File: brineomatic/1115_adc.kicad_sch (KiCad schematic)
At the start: 5 parts, among them U3 ADS1115IDGSR

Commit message: tmc2209 driver schematic checked and laid out nicely.
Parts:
- renumbered C7 to C4, C8 to C5, U3 to U1
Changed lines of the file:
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@@
 		(on_board yes)
 		(dnp no)
-		(property "Reference" "C7"
+		(property "Reference" "C4"
 			(at 184.15 80.0163 0)
 			(effects
@@
 			(project "brineomatic"
 				(path "/96477ae2-ef08-48f3-8dd4-fe4478541f68/64f85b9c-b5dc-4ec9-9075-ce977ed1cba6"
-					(reference "C7")
+					(reference "C4")
 					(unit 1)
 				)
@@
 		(on_board yes)
 		(dnp no)
-		(property "Reference" "C8"
+		(property "Reference" "C5"
 			(at 195.58 80.0163 0)
 			(effects
@@
 			(project "brineomatic"
 				(path "/96477ae2-ef08-48f3-8dd4-fe4478541f68/64f85b9c-b5dc-4ec9-9075-ce977ed1cba6"
-					(reference "C8")
+					(reference "C5")
 					(unit 1)
 				)
@@
 		(dnp no)
 		(fields_autoplaced yes)
-		(property "Reference" "#PWR020"
+		(property "Reference" "#PWR021"
 			(at 127 69.85 0)
 			(effects
@@
 			(project "brineomatic"
 				(path "/96477ae2-ef08-48f3-8dd4-fe4478541f68/64f85b9c-b5dc-4ec9-9075-ce977ed1cba6"
-					(reference "#PWR020")
+					(reference "#PWR021")
 					(unit 1)
 				)
@@
 		(dnp no)
 		(fields_autoplaced yes)
-		(property "Reference" "U3"
+		(property "Reference" "U1"
 			(at 129.1941 71.12 0)
 			(effects
@@
 			(project ""
 				(path "/96477ae2-ef08-48f3-8dd4-fe4478541f68/64f85b9c-b5dc-4ec9-9075-ce977ed1cba6"
-					(reference "U3")
+					(reference "U1")
 					(unit 1)
 				)
@@
 		(dnp no)
 		(fields_autoplaced yes)
-		(property "Reference" "#PWR021"
+		(property "Reference" "#PWR022"
 			(at 127 105.41 0)
 			(effects
@@
 			(project ""
 				(path "/96477ae2-ef08-48f3-8dd4-fe4478541f68/64f85b9c-b5dc-4ec9-9075-ce977ed1cba6"
-					(reference "#PWR021")
-					(unit 1)
-				)
+					(reference "#PWR022")
+					(unit 1)
+				)

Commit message: worked on bom for rev b prototype run
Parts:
- C4: LCSC C49678 -> (none)
- C5: LCSC C1952580 -> (none)
- R15, R16: LCSC C114561 -> (none)
- U1: LCSC (none) -> C37593
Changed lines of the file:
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@@
 			)
 		)
-		(property "LCSC" "C49678"
+		(property "LCSC" ""
 			(at 181.61 81.28 0)
 			(effects
@@
 			)
 		)
-		(property "LCSC" "C1952580"
+		(property "LCSC" ""
 			(at 193.04 81.28 0)
 			(effects
@@
 			)
 		)
-		(property "LCSC" "C114561"
+		(property "LCSC" ""
 			(at 154.94 81.28 0)
 			(effects
@@
 			)
 		)
-		(property "LCSC" ""
+		(property "LCSC" "C37593"
 			(at 127 86.36 0)
 			(effects
@@
 			)
 		)
-		(property "LCSC" "C114561"
+		(property "LCSC" ""
 			(at 165.1 81.28 0)
 			(effects

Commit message: added qwiic i2c connector
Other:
- note added: "ADC"
- title: (none) -> https://github.com/hoeken/brineomatic
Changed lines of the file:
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@@
 	(generator_version "9.0")
 	(paper "A4")
+	(title_block
+		(title "https://github.com/hoeken/brineomatic")
+		(date "2025-08-28")
+		(rev "B")
+	)
+	(rectangle
+		(start 96.52 51.435)
+		(end 207.645 109.855)
+		(stroke
+			(width 0)
+			(type default)
+		)
+		(fill
+			(type none)
+		)
+	)
+	(text "ADC"
+		(exclude_from_sim no)
+		(at 99.314 55.118 0)
+		(effects
+			(font
+				(size 2 2)
+				(thickness 0.4)
+				(bold yes)
+			)
+			(justify left)
+		)
+	)
 	(junction
 		(at 165.1 67.31)

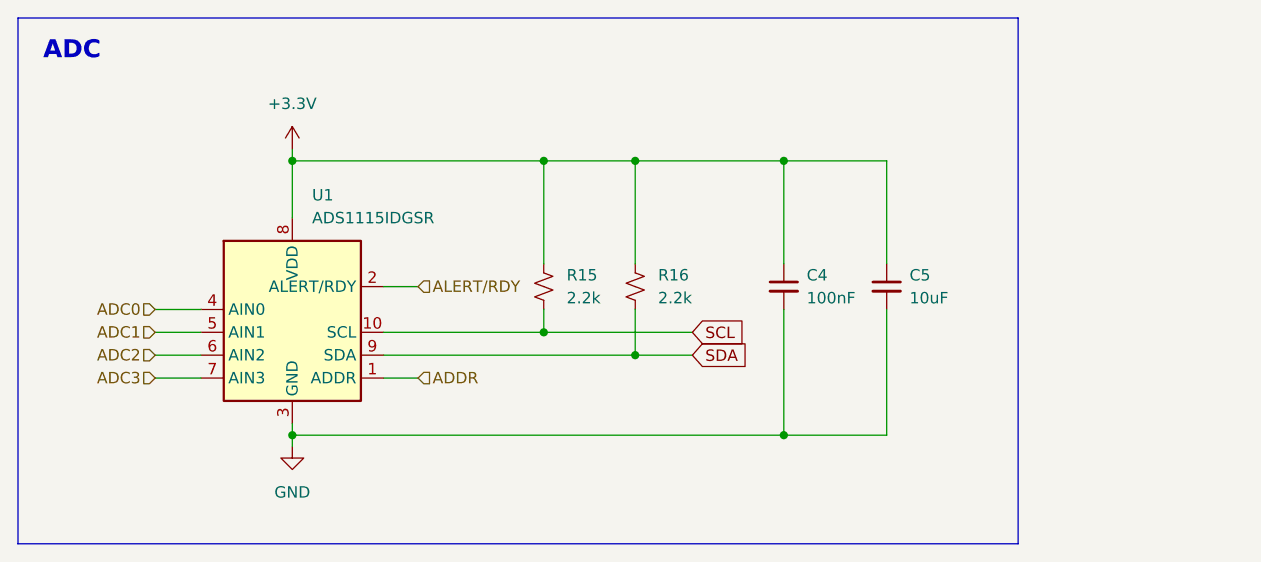
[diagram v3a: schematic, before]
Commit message: added pullup resistor to adc alert
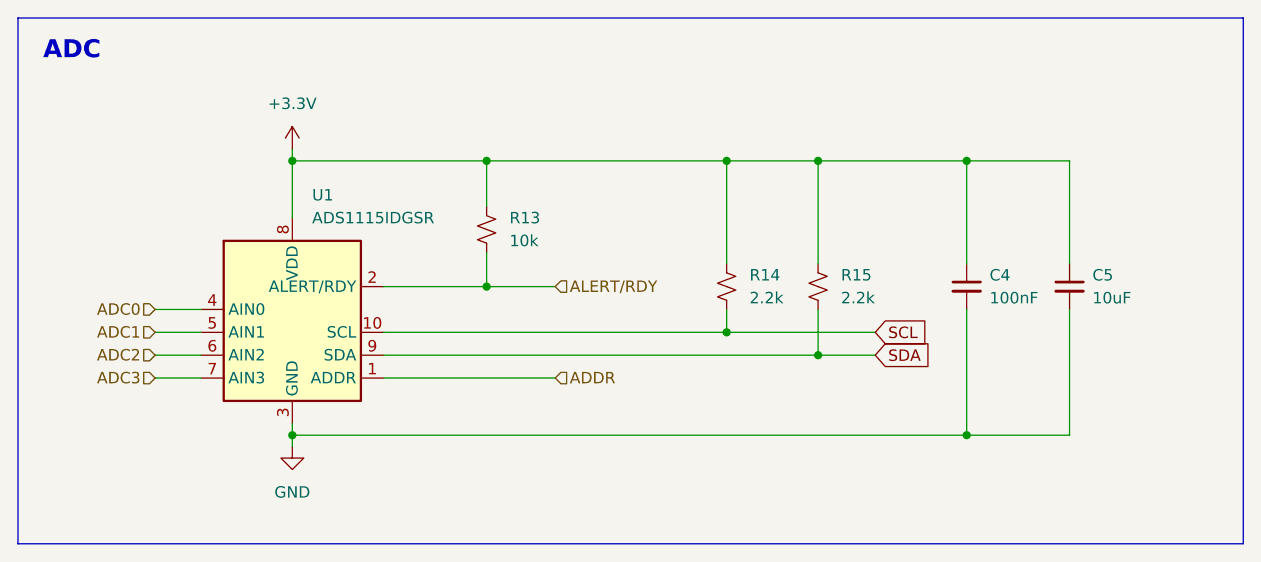
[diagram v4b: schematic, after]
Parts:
- added R13: 10k, Resistor_SMD:R_0603_1608Metric, symbol Device:R_Small_US
- renumbered R15 to R14, R16 to R15
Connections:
- net +3.3V: now also R13.2
- net ALERT/RDY: now also R13.1
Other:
- moved on the sheet: C4, C5, R14, R15

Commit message: board fully routed first pass.
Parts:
- added TP1, TP2: ~, TestPoint:TestPoint_THTPad_D1.5mm_Drill0.7mm, symbol Connector:TestPoint
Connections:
- net SCL: now also TP1.1
- net SDA: now also TP2.1

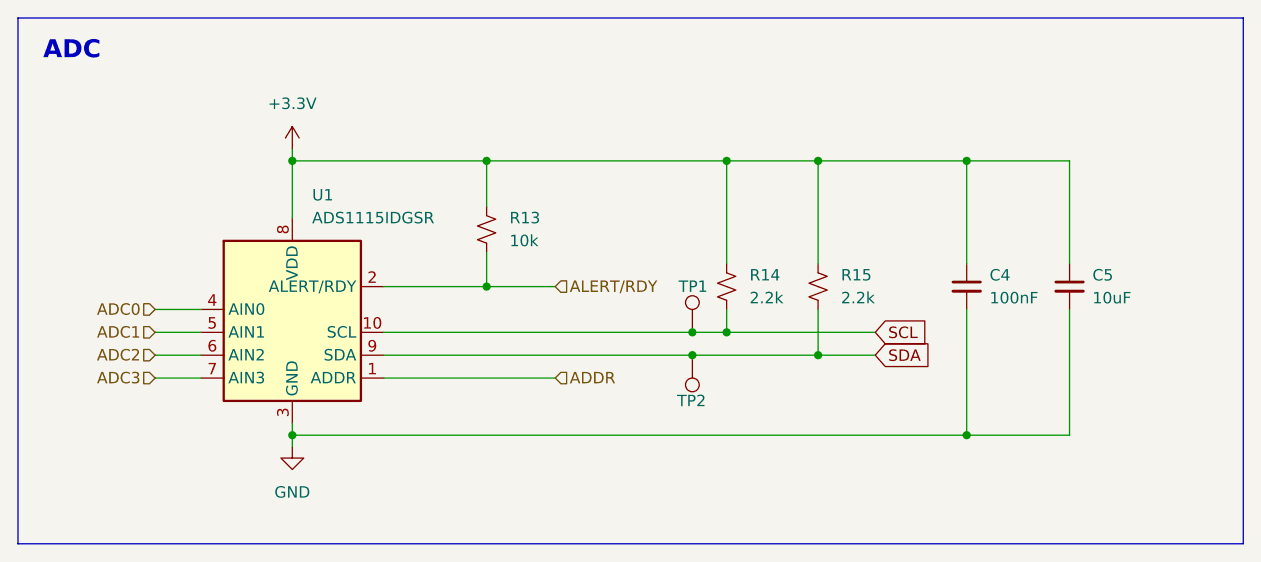
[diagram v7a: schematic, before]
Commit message: more esd protection, drc passing, silkscreen fixed
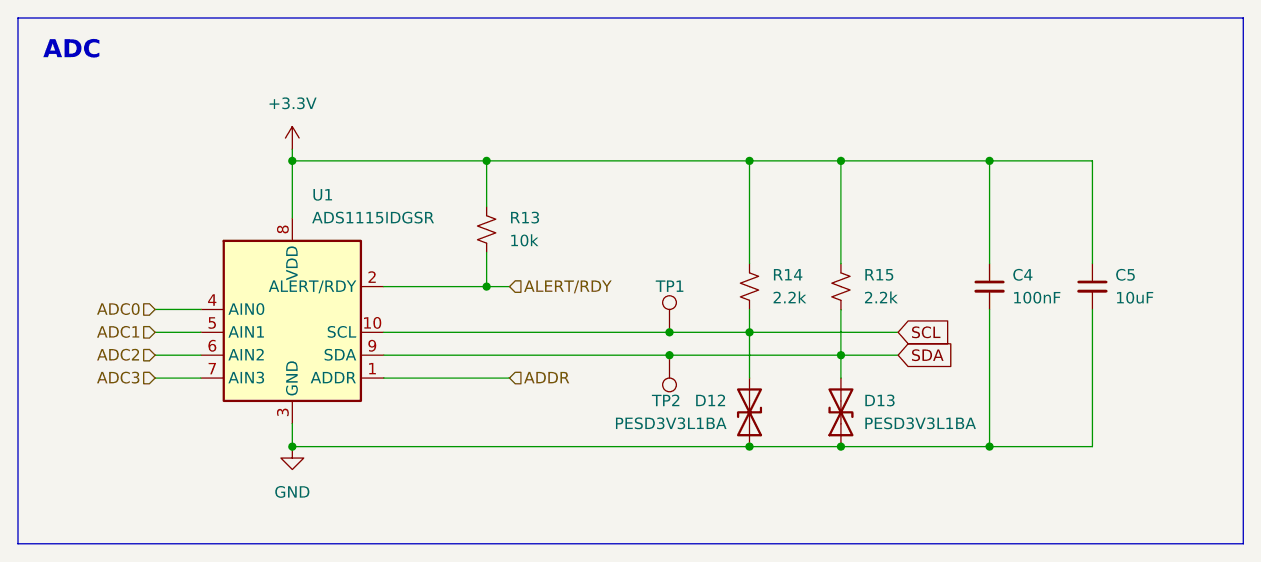
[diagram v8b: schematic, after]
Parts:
- added D12, D13: PESD3V3L1BA, Diode_SMD:D_SOD-323, symbol Device:D_TVS
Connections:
- net GND: now also D12.1 (A1), D13.1 (A1)
- net SCL: now also D12.2 (A2)
- net SDA: now also D13.2 (A2)
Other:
- moved on the sheet: C4, C5, R14, R15, TP1, TP2
